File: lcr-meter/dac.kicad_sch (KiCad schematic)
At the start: 9 parts, among them U1 KC2016Z20.0000C15XXK, U19 AD9833xRM, U20 LF353N/NOPB

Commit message: Schematic polishing
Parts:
- R22, R7: footprint (none) -> Resistor_SMD:R_0402_1005Metric
- U20: footprint N08E -> Package_DIP:DIP-8_W7.62mm
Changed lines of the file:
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@@
 			)
 		)
-		(property "Footprint" "N08E"
+		(property "Footprint" "Package_DIP:DIP-8_W7.62mm"
 			(at 146.05 109.22 0)
 			(effects
@@
 			)
 		)
-		(property "Footprint" ""
+		(property "Footprint" "Resistor_SMD:R_0402_1005Metric"
 			(at 151.13 66.04 0)
 			(effects
@@
 			)
 		)
-		(property "Footprint" "N08E"
+		(property "Footprint" "Package_DIP:DIP-8_W7.62mm"
 			(at 146.05 78.74 0)
 			(effects
@@
 			)
 		)
-		(property "Footprint" ""
+		(property "Footprint" "Resistor_SMD:R_0402_1005Metric"
 			(at 134.62 66.04 0)
 			(effects

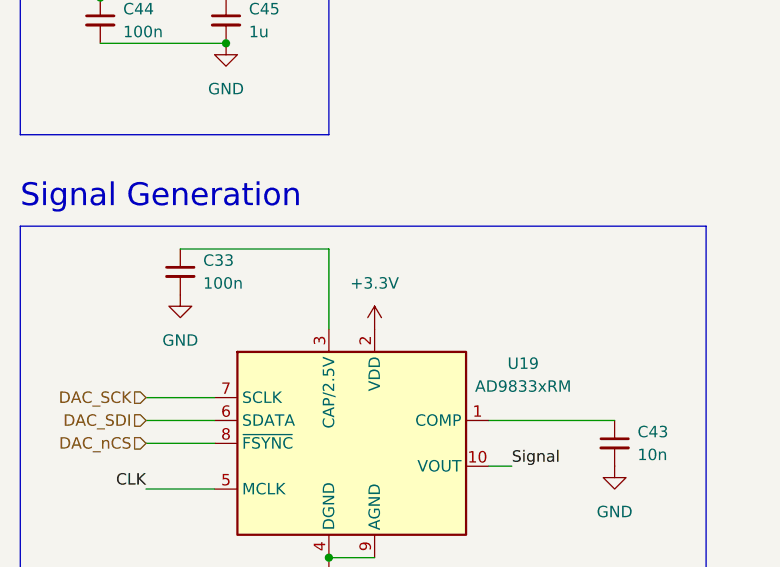
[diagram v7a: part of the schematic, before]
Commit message: Order submitteed, Mod board submitted
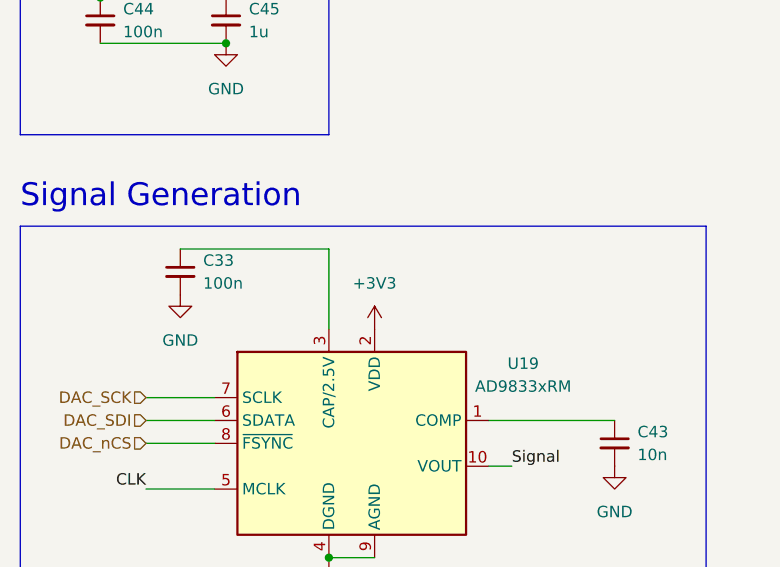
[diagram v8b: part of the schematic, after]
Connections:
- net +3.3V is gone; now on net +3V3: U19.2 (VDD)
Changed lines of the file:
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@@
 	)
 	(symbol
-		(lib_id "power:+3.3V")
+		(lib_id "power:GND")
+		(at 132.08 66.04 270)
+		(unit 1)
+		(exclude_from_sim no)
+		(in_bom yes)
+		(on_board yes)
+		(dnp no)
+		(fields_autoplaced yes)
+		(property "Reference" "#PWR071"
+			(at 125.73 66.04 0)
+			(effects
+				(font
+					(size 1.27 1.27)
+				)
+				(hide yes)
+			)
+		)
+		(property "Value" "GND"
+			(at 128.27 66.0399 90)
+			(effects
+				(font
+					(size 1.27 1.27)
+				)
+				(justify right)
+			)
+		)
+		(property "Footprint" ""
+			(at 132.08 66.04 0)
+			(effects
+				(font
+					(size 1.27 1.27)
+				)
+				(hide yes)
+			)
+		)
+		(property "Datasheet" ""
+			(at 132.08 66.04 0)
+			(effects
+				(font
+					(size 1.27 1.27)
+				)
+				(hide yes)
+			)
+		)
+		(property "Description" "Power symbol creates a global label with name \"GND\" , ground"
+			(at 132.08 66.04 0)
+			(effects
+				(font
+					(size 1.27 1.27)
+				)
+				(hide yes)
+			)
+		)
+		(pin "1"
+		)
+		(instances
+			(project ""
+				(path "/ba333b18-b098-477b-9dd4-aab7b9764d9c/46ee5347-8922-4c9f-a4b3-4d37bef42e8e"
+					(reference "#PWR071")
+					(unit 1)
+				)
+			)
+		)
+	)
+	(symbol
+		(lib_id "Device:C_Small")
+		(at 36.83 35.56 0)
+		(unit 1)
+		(exclude_from_sim no)
+		(in_bom yes)
+		(on_board yes)
+		(dnp no)
+		(fields_autoplaced yes)
+		(property "Reference" "C44"
+			(at 39.37 34.2962 0)
+			(effects
+				(font
+					(size 1.27 1.27)
+				)
+				(justify left)
+			)
+		)
+		(property "Value" "100n"
+			(at 39.37 36.8362 0)
+			(effects
+				(font
+					(size 1.27 1.27)
+				)
+				(justify left)
+			)
+		)
+		(property "Footprint" "Capacitor_SMD:C_0402_1005Metric"
+			(at 36.83 35.56 0)
+			(effects
+				(font
+					(size 1.27 1.27)
+				)
+				(hide yes)
+			)
+		)
+		(property "Datasheet" "~"
+			(at 36.83 35.56 0)
+			(effects
+				(font
+					(size 1.27 1.27)
+				)
+				(hide yes)
+			)
+		)
+		(property "Description" "Unpolarized capacitor, small symbol"
+			(at 36.83 35.56 0)
+			(effects
+				(font
+					(size 1.27 1.27)
+				)
+				(hide yes)
+			)
+		)
+		(pin "1"
+		)
+		(pin "2"
+		)
+		(instances
+			(project "lcr-meter"
+				(path "/ba333b18-b098-477b-9dd4-aab7b9764d9c/46ee5347-8922-4c9f-a4b3-4d37bef42e8e"
+					(reference "C44")
+					(unit 1)
+				)
+			)
+		)
+	)
+	(symbol
+		(lib_id "power:+3V3")
+		(at 36.83 33.02 0)
+		(unit 1)
+		(exclude_from_sim no)
+		(in_bom yes)
+		(on_board yes)
+		(dnp no)
+		(fields_autoplaced yes)
+		(property "Reference" "#PWR059"
+			(at 36.83 36.83 0)
+			(effects
+				(font
+					(size 1.27 1.27)
+				)
+				(hide yes)
+			)
+		)
+		(property "Value" "+3V3"
+			(at 36.83 27.94 0)
+			(effects
+				(font
+					(size 1.27 1.27)
+				)
+			)
+		)
+		(property "Footprint" ""
+			(at 36.83 33.02 0)
+			(effects
+				(font
+					(size 1.27 1.27)
+				)
+				(hide yes)
+			)
+		)
+		(property "Datasheet" ""
+			(at 36.83 33.02 0)
+			(effects
+				(font
+					(size 1.27 1.27)
+				)
+				(hide yes)
+			)
+		)
+		(property "Description" "Power symbol creates a global label with name \"+3V3\""
+			(at 36.83 33.02 0)
+			(effects
+				(font
+					(size 1.27 1.27)
+				)
+				(hide yes)
+			)
+		)
+		(pin "1"
+		)
+		(instances
+			(project ""
+				(path "/ba333b18-b098-477b-9dd4-aab7b9764d9c/46ee5347-8922-4c9f-a4b3-4d37bef42e8e"
+					(reference "#PWR059")
+					(unit 1)
+				)
+			)
+		)
+	)
+	(symbol
+		(lib_id "power:+3V3")
 		(at 67.31 69.85 0)
 		(unit 1)
@@
 			)
 		)
-		(property "Value" "+3.3V"
+		(property "Value" "+3V3"
 			(at 67.31 64.77 0)
 			(effects
@@
 			)
 		)
-		(property "Description" "Power symbol creates a global label with name \"+3.3V\""
+		(property "Description" "Power symbol creates a global label with name \"+3V3\""
 			(at 67.31 69.85 0)
 			(effects
@@
 					(unit 1)
 				)
-			)
-		)
-	)
-	(symbol
-		(lib_id "power:GND")
-		(at 132.08 66.04 270)
-		(unit 1)
-		(exclude_from_sim no)
-		(in_bom yes)
-		(on_board yes)
-		(dnp no)
-		(fields_autoplaced yes)
-		(property "Reference" "#PWR071"
-			(at 125.73 66.04 0)
-			(effects
-				(font
-					(size 1.27 1.27)
-				)
-				(hide yes)
-			)
-		)
-		(property "Value" "GND"
-			(at 128.27 66.0399 90)
-			(effects
-				(font
-					(size 1.27 1.27)
-				)
-				(justify right)
-			)
-		)
-		(property "Footprint" ""
-			(at 132.08 66.04 0)
-			(effects
-				(font
-					(size 1.27 1.27)
-				)
-				(hide yes)
-			)
-		)
-		(property "Datasheet" ""
-			(at 132.08 66.04 0)
-			(effects
-				(font
-					(size 1.27 1.27)
-				)
-				(hide yes)
-			)
-		)
-		(property "Description" "Power symbol creates a global label with name \"GND\" , ground"
-			(at 132.08 66.04 0)
-			(effects
-				(font
-					(size 1.27 1.27)
-				)
-				(hide yes)
-			)
-		)
-		(pin "1"
-		)
-		(instances
-			(project ""
-				(path "/ba333b18-b098-477b-9dd4-aab7b9764d9c/46ee5347-8922-4c9f-a4b3-4d37bef42e8e"
-					(reference "#PWR071")
-					(unit 1)
-				)
-			)
-		)
-	)
-	(symbol
-		(lib_id "Device:C_Small")
-		(at 36.83 35.56 0)
-		(unit 1)
-		(exclude_from_sim no)
-		(in_bom yes)
-		(on_board yes)
-		(dnp no)
-		(fields_autoplaced yes)
-		(property "Reference" "C44"
-			(at 39.37 34.2962 0)
-			(effects
-				(font
-					(size 1.27 1.27)
-				)
-				(justify left)
-			)
-		)
-		(property "Value" "100n"
-			(at 39.37 36.8362 0)
-			(effects
-				(font
-					(size 1.27 1.27)
-				)
-				(justify left)
-			)
-		)
-		(property "Footprint" "Capacitor_SMD:C_0402_1005Metric"
-			(at 36.83 35.56 0)
-			(effects
-				(font
-					(size 1.27 1.27)
-				)
-				(hide yes)
-			)
-		)
-		(property "Datasheet" "~"
-			(at 36.83 35.56 0)
-			(effects
-				(font
-					(size 1.27 1.27)
-				)
-				(hide yes)
-			)
-		)
-		(property "Description" "Unpolarized capacitor, small symbol"
-			(at 36.83 35.56 0)
-			(effects
-				(font
-					(size 1.27 1.27)
-				)
-				(hide yes)
-			)
-		)
-		(pin "1"
-		)
-		(pin "2"
-		)
-		(instances
-			(project "lcr-meter"
-				(path "/ba333b18-b098-477b-9dd4-aab7b9764d9c/46ee5347-8922-4c9f-a4b3-4d37bef42e8e"
-					(reference "C44")
-					(unit 1)
-				)
-			)
-		)
-	)
-	(symbol
-		(lib_id "power:+3V3")
-		(at 36.83 33.02 0)
-		(unit 1)
-		(exclude_from_sim no)
-		(in_bom yes)
-		(on_board yes)
-		(dnp no)
-		(fields_autoplaced yes)
-		(property "Reference" "#PWR059"
-			(at 36.83 36.83 0)
-			(effects
-				(font
-					(size 1.27 1.27)
-				)
-				(hide yes)
-			)
-		)
-		(property "Value" "+3V3"
-			(at 36.83 27.94 0)
-			(effects
-				(font
-					(size 1.27 1.27)
-				)
-			)
-		)
-		(property "Footprint" ""
-			(at 36.83 33.02 0)
-			(effects
-				(font
-					(size 1.27 1.27)
-				)
-				(hide yes)
-			)
-		)
-		(property "Datasheet" ""
-			(at 36.83 33.02 0)
-			(effects
-				(font
-					(size 1.27 1.27)
-				)
-				(hide yes)
-			)
-		)
-		(property "Description" "Power symbol creates a global label with name \"+3V3\""
-			(at 36.83 33.02 0)
-			(effects
-				(font
-					(size 1.27 1.27)
-				)
-				(hide yes)
-			)
-		)
-		(pin "1"
-		)
-		(instances
-			(project ""
-				(path "/ba333b18-b098-477b-9dd4-aab7b9764d9c/46ee5347-8922-4c9f-a4b3-4d37bef42e8e"
-					(reference "#PWR059")
-					(unit 1)
-				)
